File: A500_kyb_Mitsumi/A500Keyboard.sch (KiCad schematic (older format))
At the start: 34 parts, among them IC1 6570-036, IC2- 74LS27, IC3- 74LS123, IC4 NE555, J1 KYB_MATRIX, J2 8-PIN SIL, Q1 BC485C, Q2 BC485C, Y1 3.000 MHz

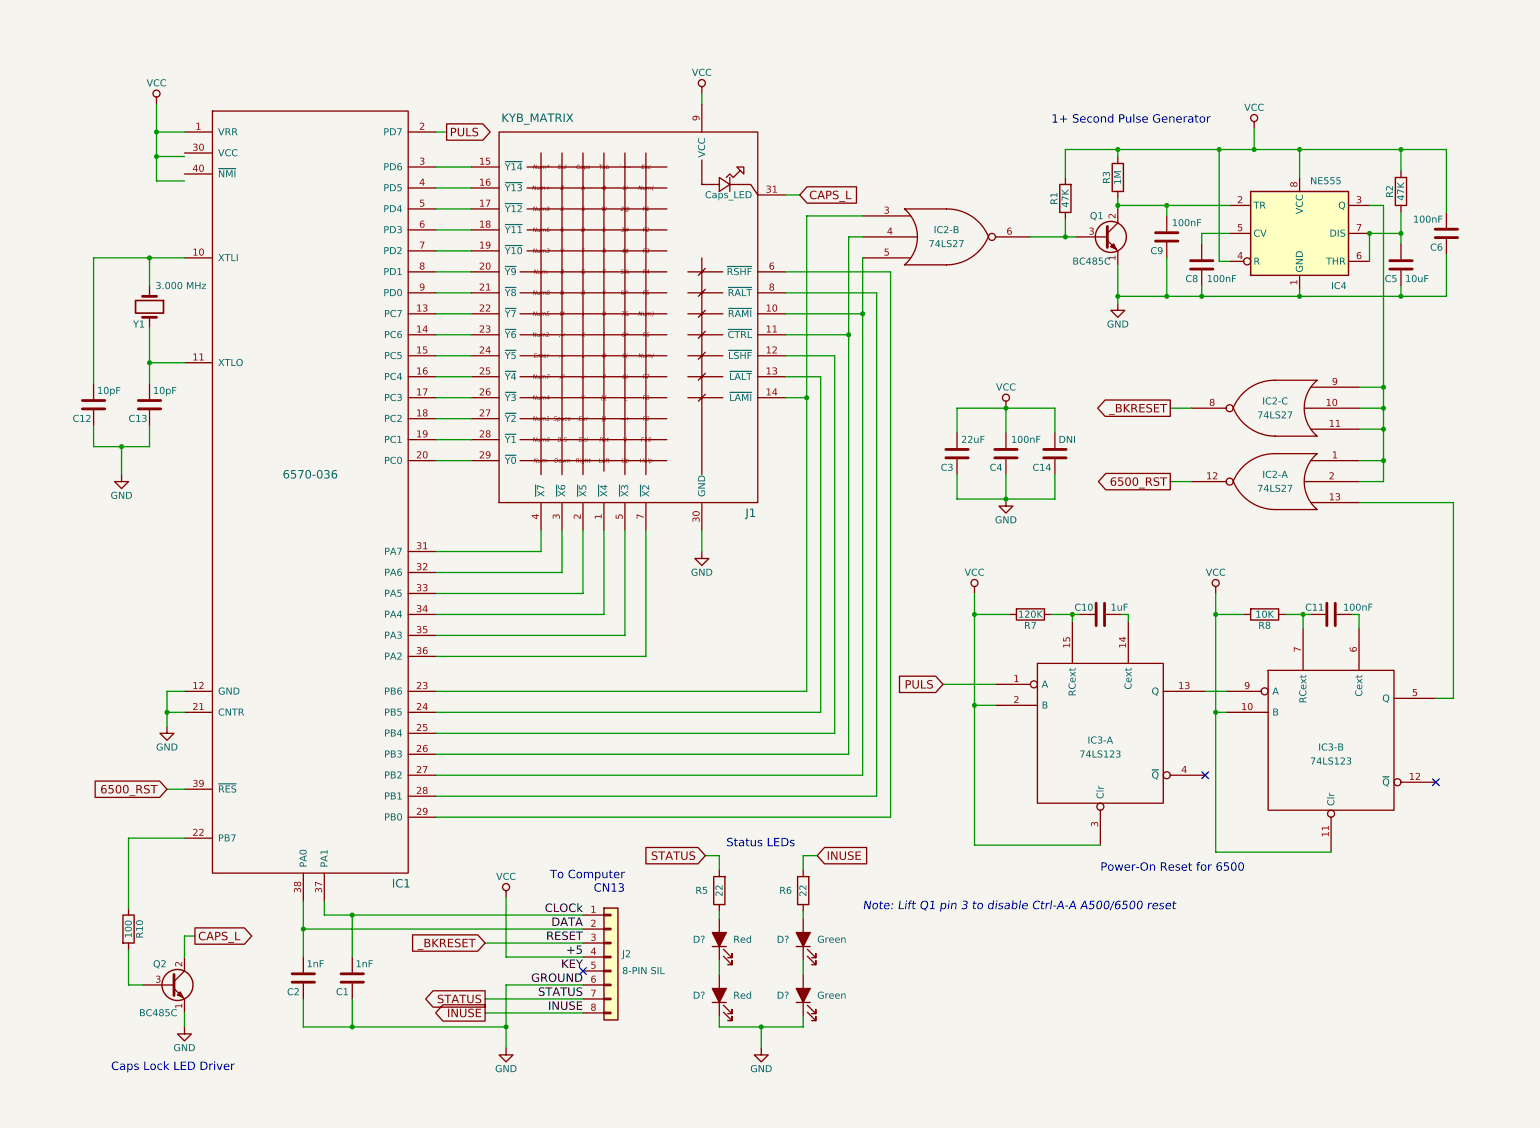
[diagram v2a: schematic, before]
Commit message: MOS 6570 pins fixes, renames, spacing and additional labelling. - MOS 6570:   - Renamed pins to not include their in-circuit function but just their name as specified by MOS. Labels were moved to wire/pin junctions.   - Fixed the spacing of a few pins so that all adjacent pins have the same spacing. - Circuit   - Added wire/pin junctions labels around the 6570 to indicate usage (were previously part of the pin labels).   - Fixed a duplicate label pointed out by solarmon on the English Amiga Board (http://eab.abime.net/showpost.php?p=1391450&postcount=16).   - Renamed these labels to names used by Commodore (when available) or on https://www.amiga-stuff.com/hardware/6500_1.html when they did not conflict with the Commodore ones.
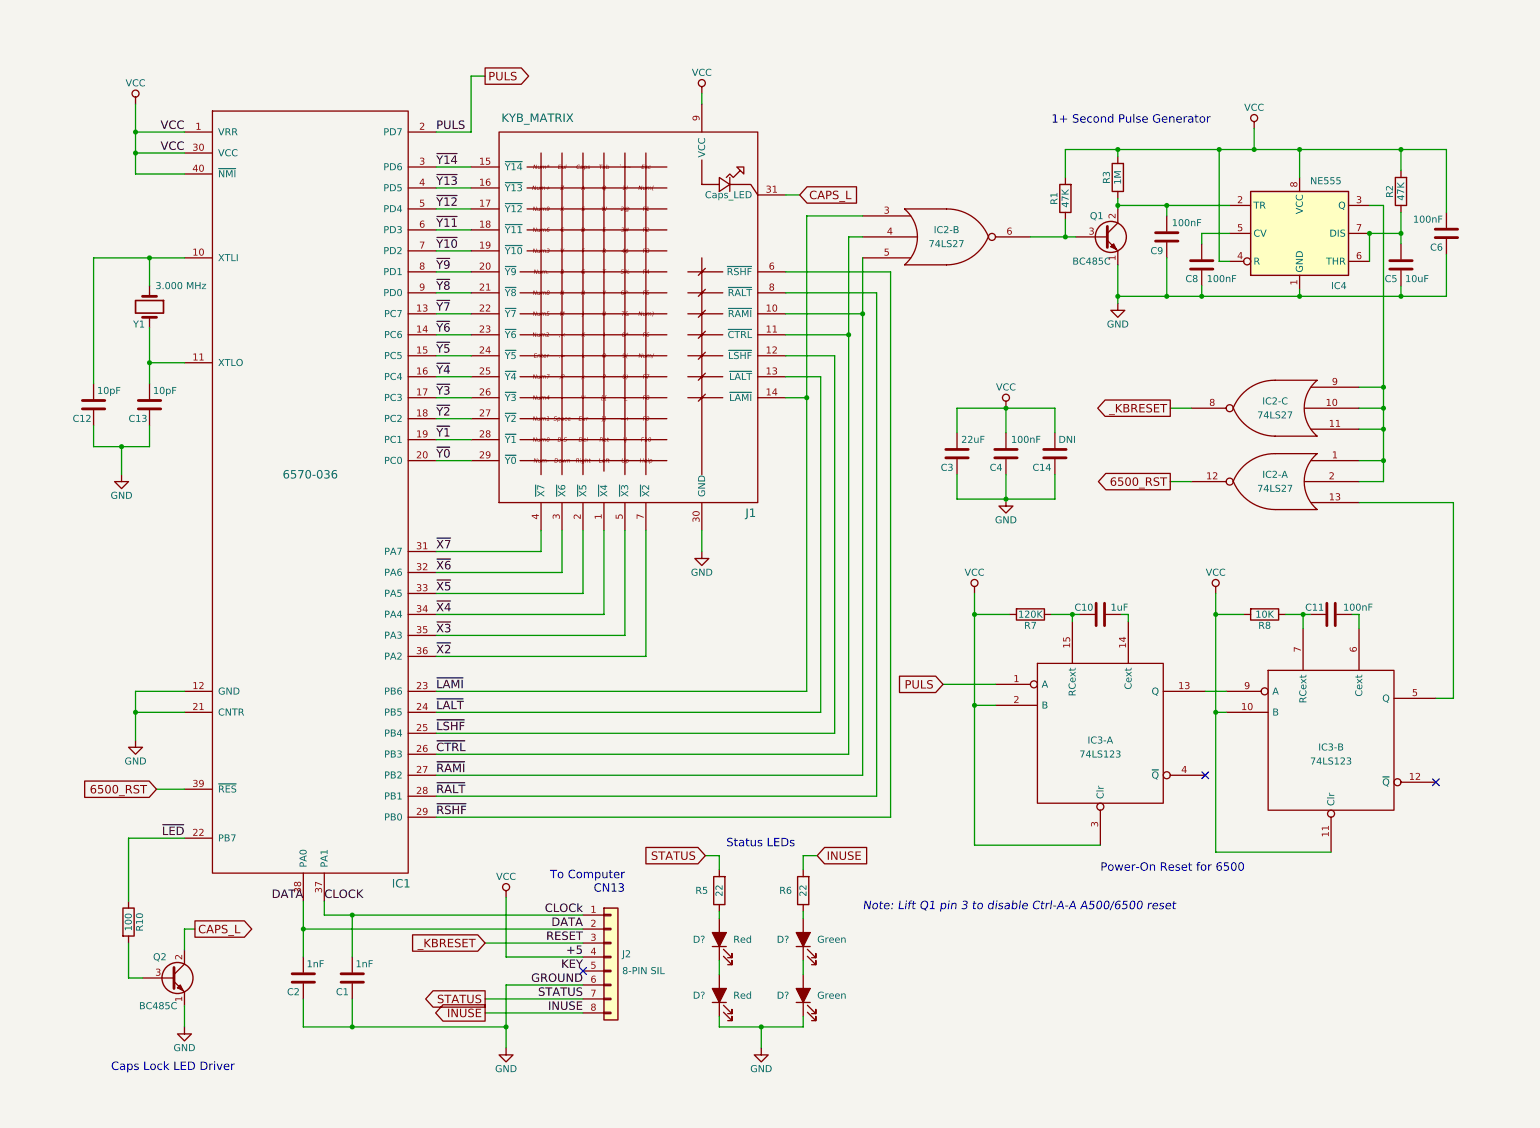
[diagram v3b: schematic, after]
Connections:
- net VCC: now also IC1.30 (VCC), IC1.40 (~NMI)
- net ~X4: now reaches IC1.34 (PA4), J1.1 (~X4)
- net ~RAMI: now reaches IC1.27 (PB2), IC2-.5, J1.10 (~RAMI)
- net ~CTRL: now reaches IC1.26 (PB3), IC2-.4, J1.11 (~CTRL)
- net ~LSHF: now reaches IC1.25 (PB4), J1.12 (~LSHF)
- net ~LALT: now reaches IC1.24 (PB5), J1.13 (~LALT)
- net ~LAMI: now reaches IC1.23 (PB6), IC2-.3, J1.14 (~LAMI)
- net ~Y14: now reaches IC1.3 (PD6), J1.15 (~Y14)
- net ~Y13: now reaches IC1.4 (PD5), J1.16 (~Y13)
- net ~Y12: now reaches IC1.5 (PD4), J1.17 (~Y12)
- net ~Y11: now reaches IC1.6 (PD3), J1.18 (~Y11)
- net ~Y10: now reaches IC1.7 (PD2), J1.19 (~Y10)
- net ~X5: now reaches IC1.33 (PA5), J1.2 (~X5)
- net ~Y9: now reaches IC1.8 (PD1), J1.20 (~Y9)
- net ~Y8: now reaches IC1.9 (PD0), J1.21 (~Y8)
- net ~Y7: now reaches IC1.13 (PC7), J1.22 (~Y7)
- net ~Y6: now reaches IC1.14 (PC6), J1.23 (~Y6)
- net ~Y5: now reaches IC1.15 (PC5), J1.24 (~Y5)
- net ~Y4: now reaches IC1.16 (PC4), J1.25 (~Y4)
- net ~Y3: now reaches IC1.17 (PC3), J1.26 (~Y3)
- net ~Y2: now reaches IC1.18 (PC2), J1.27 (~Y2)
- net ~Y1: now reaches IC1.19 (PC1), J1.28 (~Y1)
- net ~Y0: now reaches IC1.20 (PC0), J1.29 (~Y0)
- net ~X6: now reaches IC1.32 (PA6), J1.3 (~X6)
- net ~X7: now reaches IC1.31 (PA7), J1.4 (~X7)
- net ~X3: now reaches IC1.35 (PA3), J1.5 (~X3)
- net ~RSHF: now reaches IC1.29 (PB0), J1.6 (~RSHF)
- net ~X2: now reaches IC1.36 (PA2), J1.7 (~X2)
- net ~RALT: now reaches IC1.28 (PB1), J1.8 (~RALT)
- net ~LED: now reaches IC1.22 (PB7), R10.1
- net CLOCk renamed CLOCK
- net _BKRESET renamed _KBRESET
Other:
- moved on the sheet: Q2, R10
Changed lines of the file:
@@
 $EndDescr
-$Comp
-L A500_Parts:KYB_MATRIX J1
-U 1 1 5A78FF17
-P 4600 2450
-F 0 "J1" H 5400 1025 60  0000 C CNN
-F 1 "KYB_MATRIX" H 3875 3850 60  0000 C CNN
-F 2 "" H 3850 1675 60  0001 C CNN
-F 3 "" H 3850 1675 60  0001 C CNN
-	1    4600 2450
-	1    0    0    -1
-$EndComp
 $Comp
 L power:VCC #PWR?
 U 1 1 5A7904F6
-P 1150 950
-F 0 "#PWR?" H 1150 800 50  0001 C CNN
-F 1 "VCC" H 1150 1100 50  0000 C CNN
-F 2 "" H 1150 950 50  0001 C CNN
-F 3 "" H 1150 950 50  0001 C CNN
-	1    1150 950
-	1    0    0    -1
-$EndComp
-$Comp
-L Device:Crystal Y1
-U 1 1 5A790564
-P 1100 2400
-F 0 "Y1" V 1225 2325 50  0000 C CNN
-F 1 "3.000 MHz" V 950 2625 50  0000 C CNN
-F 2 "" H 1100 2400 50  0001 C CNN
-F 3 "" H 1100 2400 50  0001 C CNN
-	1    1100 2400
-	0    1    1    0
+P 1000 950
+F 0 "#PWR?" H 1000 800 50  0001 C CNN
+F 1 "VCC" H 1000 1100 50  0000 C CNN
+F 2 "" H 1000 950 50  0001 C CNN
+F 3 "" H 1000 950 50  0001 C CNN
+	1    1000 950
+	1    0    0    -1
 $EndComp
 $Comp
@@
 $Comp
 L power:GND #PWR?
-U 1 1 5A7906CF
-P 1225 5400
-F 0 "#PWR?" H 1225 5150 50  0001 C CNN
-F 1 "GND" H 1225 5250 50  0000 C CNN
-F 2 "" H 1225 5400 50  0001 C CNN
-F 3 "" H 1225 5400 50  0001 C CNN
-	1    1225 5400
-	1    0    0    -1
-$EndComp
-$Comp
-L power:GND #PWR?
 U 1 1 5A790774
 P 900 3600
@@
 L Device:R R10
 U 1 1 5A7A6032
-P 950 6850
-F 0 "R10" V 1030 6850 50  0000 C CNN
-F 1 "100" V 950 6850 50  0000 C CNN
-F 2 "" V 880 6850 50  0001 C CNN
-F 3 "" H 950 6850 50  0001 C CNN
-	1    950  6850
+P 950 6800
+F 0 "R10" V 1030 6800 50  0000 C CNN
+F 1 "100" V 950 6800 50  0000 C CNN
+F 2 "" V 880 6800 50  0001 C CNN
+F 3 "" H 950 6800 50  0001 C CNN
+	1    950  6800
 	1    0    0    -1
 $EndComp
@@
 L Device:Q_NPN_ECB Q2
 U 1 1 5A7A621D
-P 1250 7250
-F 0 "Q2" H 1125 7400 50  0000 L CNN
-F 1 "BC485C" H 1025 7050 50  0000 L CNN
-F 2 "" H 1450 7350 50  0001 C CNN
-F 3 "" H 1250 7250 50  0001 C CNN
-	1    1250 7250
+P 1250 7200
+F 0 "Q2" H 1125 7350 50  0000 L CNN
+F 1 "BC485C" H 1025 7000 50  0000 L CNN
+F 2 "" H 1450 7300 50  0001 C CNN
+F 3 "" H 1250 7200 50  0001 C CNN
+	1    1250 7200
 	1    0    0    -1
 $EndComp
@@
 	-1   0    0    -1
 $EndComp
-Text GLabel 1425 6900 2    60   Output ~ 0
+Text GLabel 1425 6850 2    60   Output ~ 0
 CAPS_L
 Text GLabel 5750 1600 2    60   Input ~ 0
 CAPS_L
-Text GLabel 1225 5850 0    60   Input ~ 0
+Text GLabel 1150 5850 0    60   Input ~ 0
 6500_RST
 Text GLabel 8400 3650 0    60   Output ~ 0
 6500_RST
 Text GLabel 8400 3125 0    60   Output ~ 0
-_BKRESET
-Text GLabel 3225 1150 2    60   Output ~ 0
-PULS
+_KBRESET
 $Comp
 L Device:R R1
@@
 Power-On Reset for 6500
 Wire Wire Line
-	1150 950  1150 1150
-Wire Wire Line
-	1150 1150 1150 1325
-Wire Wire Line
-	1150 1325 1150 1500
-Connection ~ 1150 1150
-Connection ~ 1150 1325
-Wire Wire Line
-	1100 2250 1100 2050
+	1000 950  1000 1150
+Wire Wire Line
+	1000 1150 1000 1300
+Wire Wire Line
+	1000 1300 1000 1450
+Connection ~ 1000 1150
+Connection ~ 1000 1300
 Wire Wire Line
 	700  2050 1100 2050
-Wire Wire Line
-	1100 2550 1100 2800
 Connection ~ 1100 2050
 Wire Wire Line
@@
 	900  3600 900  3400
 Connection ~ 900  3400
-Wire Wire Line
-	1225 5150 1225 5300
-Wire Wire Line
-	1225 5300 1225 5400
-Connection ~ 1225 5300
 Wire Wire Line
 	3900 4150 3900 4000
@@
 Connection ~ 5800 3050
 Wire Wire Line
-	1350 7450 1350 7550
+	1350 7400 1350 7550
 Wire Wire Line
 	7650 1275 7650 1475
@@
 	8025 2325 8025 2375
 Wire Wire Line
-	1425 6900 1350 6900
-Wire Wire Line
-	1350 6900 1350 7050
+	1425 6850 1350 6850
+Wire Wire Line
+	1350 6850 1350 7000
 Wire Wire Line
 	8025 1625 8025 1675
@@
 Connection ~ 8725 5300
 Wire Wire Line
-	1050 7250 950  7250
-Wire Wire Line
-	950  7250 950  7000
-Wire Wire Line
-	950  6700 950  6200
+	1050 7200 950  7200
+Wire Wire Line
+	950  7200 950  6950
+Wire Wire Line
+	950  6650 950  6200
 Wire Wire Line
 	6200 1750 5800 1750
@@
 $EndComp
 Wire Wire Line
-	1225 5850 1350 5850
+	1150 5850 1350 5850
 Wire Wire Line
 	5800 5150 3150 5150
@@
 	950  6200 1350 6200
 Wire Wire Line
-	1350 5150 1225 5150
-Wire Wire Line
 	3150 4150 3900 4150
 Wire Wire Line
-	1350 5300 1225 5300
-Wire Wire Line
 	1100 2800 1350 2800
 Wire Wire Line
-	1150 1500 1350 1500
-Wire Wire Line
-	1150 1325 1350 1325
+	1000 1450 1350 1450
+Wire Wire Line
+	1000 1300 1350 1300
 Wire Wire Line
 	3150 1400 3400 1400
 Wire Wire Line
-	3225 1150 3150 1150
-Wire Wire Line
-	1350 1150 1150 1150
+	1350 1150 1000 1150
 $Comp
 L Device:C C1
@@
 $EndComp
 Text GLabel 3500 6950 0    60   Input ~ 0
-_BKRESET
+_KBRESET
 Wire Wire Line
 	2200 7550 2550 7550
@@
 Wire Wire Line
 	7400 1900 7650 1900
+Text Label 3150 1400 0    60   ~ 0
+~Y14
+Text Label 3150 1550 0    60   ~ 0
+~Y13
+Text Label 3150 1700 0    60   ~ 0
+~Y12
+Text Label 3150 1850 0    60   ~ 0
+~Y11
+Text Label 3150 2000 0    60   ~ 0
+~Y10
+Text Label 3150 2150 0    60   ~ 0
+~Y9
+Text Label 3150 2300 0    60   ~ 0
+~Y8
+Text Label 3150 2450 0    60   ~ 0
+~Y7
+Text Label 3150 2600 0    60   ~ 0
+~Y6
+Text Label 3150 2750 0    60   ~ 0
+~Y5
+Text Label 3150 2900 0    60   ~ 0
+~Y4
+Text Label 3150 3050 0    60   ~ 0
+~Y3
+Text Label 3150 3200 0    60   ~ 0
+~Y2
+Text Label 3150 3350 0    60   ~ 0
+~Y1
+Text Label 3150 3500 0    60   ~ 0
+~Y0
+Text GLabel 3500 750  2    60   Output ~ 0
+PULS
+$Comp
+L A500_Parts:KYB_MATRIX J1
+U 1 1 5A78FF17
+P 4600 2450
+F 0 "J1" H 5400 1025 60  0000 C CNN
+F 1 "KYB_MATRIX" H 3875 3850 60  0000 C CNN
+F 2 "" H 3850 1675 60  0001 C CNN
+F 3 "" H 3850 1675 60  0001 C CNN
+	1    4600 2450
+	1    0    0    -1
+$EndComp
+Wire Wire Line
+	3150 1150 3400 1150
+Wire Wire Line
+	3400 1150 3400 750
+Wire Wire Line
+	3400 750  3500 750
+Text Label 3150 1150 0    60   ~ 0
+PULS
+Text Label 3150 4150 0    60   ~ 0
+~X7
+Text Label 3150 4300 0    60   ~ 0
+~X6
+Text Label 3150 4450 0    60   ~ 0
+~X5
+Text Label 3150 4600 0    60   ~ 0
+~X4
+Text Label 3150 4750 0    60   ~ 0
+~X3
+Text Label 3150 4900 0    60   ~ 0
+~X2
+Text Label 3150 5150 0    60   ~ 0
+~LAMI
+Text Label 3150 5300 0    60   ~ 0
+~LALT
+Text Label 3150 5450 0    60   ~ 0
+~LSHF
+Text Label 3150 5600 0    60   ~ 0
+~CTRL
+Text Label 3150 5750 0    60   ~ 0
+~RAMI
+Text Label 3150 5900 0    60   ~ 0
+~RALT
+Text Label 3150 6050 0    60   ~ 0
+~RSHF
+Wire Wire Line
+	1350 5300 1000 5300
+Wire Wire Line
+	1350 5150 1000 5150
+Connection ~ 1000 5300
+Wire Wire Line
+	1000 5300 1000 5500
+Wire Wire Line
+	1000 5150 1000 5300
+$Comp
+L power:GND #PWR?
+U 1 1 5A7906CF
+P 1000 5500
+F 0 "#PWR?" H 1000 5250 50  0001 C CNN
+F 1 "GND" H 1000 5350 50  0000 C CNN
+F 2 "" H 1000 5500 50  0001 C CNN
+F 3 "" H 1000 5500 50  0001 C CNN
+	1    1000 5500
+	1    0    0    -1
+$EndComp
+Text Label 1350 6200 2    60   ~ 0
+~LED
+Wire Wire Line
+	1100 2550 1100 2800
+Wire Wire Line
+	1100 2250 1100 2050
+$Comp
+L Device:Crystal Y1
+U 1 1 5A790564
+P 1100 2400
+F 0 "Y1" V 1225 2325 50  0000 C CNN
+F 1 "3.000 MHz" V 950 2625 50  0000 C CNN
+F 2 "" H 1100 2400 50  0001 C CNN
+F 3 "" H 1100 2400 50  0001 C CNN
+	1    1100 2400
+	0    1    1    0
+$EndComp
+Text Label 1350 1150 2    60   ~ 0
+VCC
+Text Label 1350 1300 2    60   ~ 0
+VCC
+Text Label 2350 6650 0    60   ~ 0
+CLOCK
+Text Label 2200 6650 2    60   ~ 0
+DATA
 $EndSCHEMATC
